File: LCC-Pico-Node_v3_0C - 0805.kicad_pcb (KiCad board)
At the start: 4 copper layers, 100 x 82 mm, 89 parts, among them IC1 TPS54228DR, IC2 MCP2518FD, IC3 MCP2562FD, IC5 256Kb, IC6 TPS54228DR, J1 RJ45, J12 Power Sel, J15 Analog I/O, J16 NVM Power Sel, J2 RJ45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

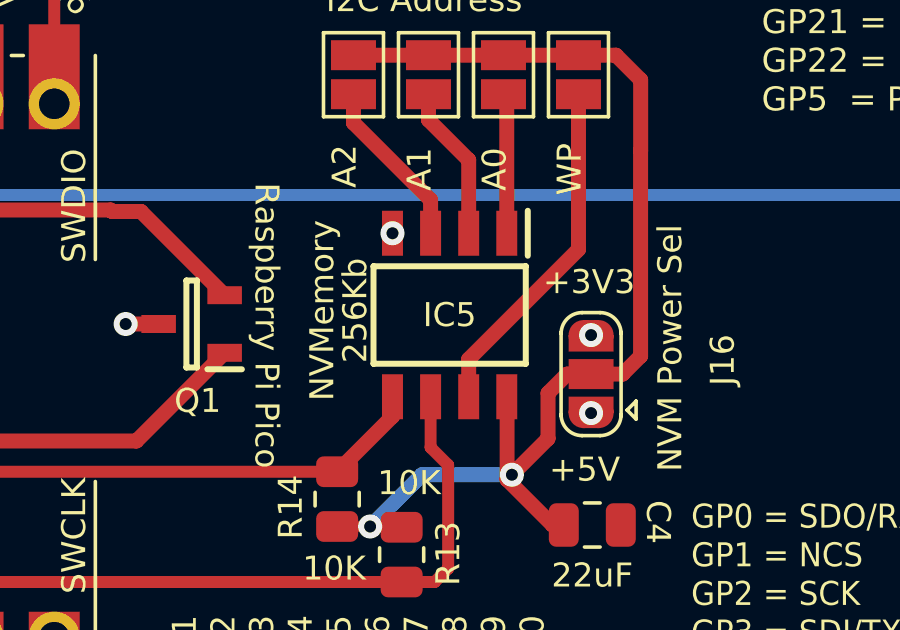
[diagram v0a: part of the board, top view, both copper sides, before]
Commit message: Fixed a problem file
a footprint got rotated by accident
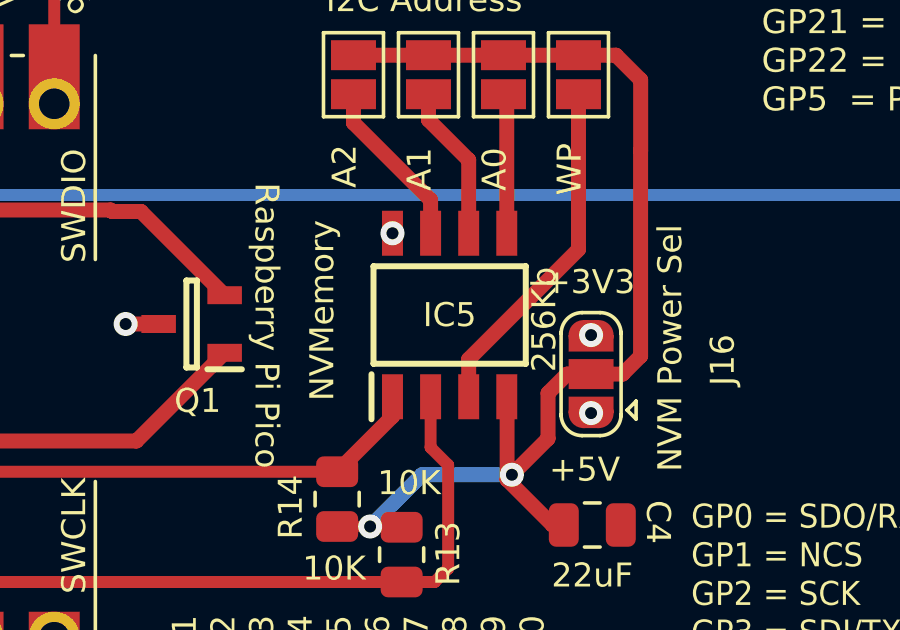
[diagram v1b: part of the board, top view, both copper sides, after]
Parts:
- turned IC5 to 90 degrees
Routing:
- net GND: track 84.0 -> 44.9 mm, vias 36 -> 35
- net Net-(IC5-VSS): track 0.00 -> 39.0 mm, vias 1 -> 2
